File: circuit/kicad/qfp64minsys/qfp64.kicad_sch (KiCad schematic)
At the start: 0 parts

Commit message: Progress
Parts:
- added C1, C2, C4: 100nF, Capacitor_SMD:C_0805_2012Metric_Pad1.18x1.45mm_HandSolder, symbol Device:C
- added C3: 100uF, Capacitor_THT:CP_Radial_D4.0mm_P1.50mm, symbol Device:C_Polarized
- added C5, C6, C7, C8: 10nF, Capacitor_SMD:C_0805_2012Metric_Pad1.18x1.45mm_HandSolder, symbol Device:C
- added C9: 4u7F, Capacitor_Tantalum_SMD:CP_EIA-3216-18_Kemet-A, symbol Device:C
- added D1: RED, LED_SMD:LED_0805_2012Metric_Pad1.15x1.40mm_HandSolder, symbol Device:LED
- added D2: YELLOW, LED_SMD:LED_0805_2012Metric_Pad1.15x1.40mm_HandSolder, symbol Device:LED
- added J1, J6: Conn_01x05_Pin, Connector_PinSocket_2.54mm:PinSocket_1x05_P2.54mm_Vertical, symbol Connector:Conn_01x05_Pin
- added J10, J7, J9: Conn_01x09_Pin, Connector_PinSocket_2.54mm:PinSocket_1x09_P2.54mm_Vertical, symbol Connector:Conn_01x09_Pin
- added J2, J3: USB_B_Mini, Connector_USB:USB_Mini-B_Wuerth_65100516121_Horizontal, symbol Connector:USB_B_Mini
- added J4, J5: Conn_01x03_Pin, Connector_PinSocket_2.54mm:PinSocket_1x03_P2.54mm_Vertical, symbol Connector:Conn_01x03_Pin
- added J8: Conn_01x12_Pin, Connector_PinSocket_2.54mm:PinSocket_1x12_P2.54mm_Vertical, symbol Connector:Conn_01x12_Pin
- added JP1, JP2, JP3, JP4, JP5: SolderJumper_2_Open, Jumper:SolderJumper-2_P1.3mm_Open_TrianglePad1.0x1.5mm, symbol Jumper:SolderJumper_2_Open
- added R1, R2, R3, R6: 10K, Resistor_SMD:R_0805_2012Metric_Pad1.20x1.40mm_HandSolder, symbol Device:R
- added R4, R5: 330, Resistor_SMD:R_0805_2012Metric_Pad1.20x1.40mm_HandSolder, symbol Device:R
- added SW1, SW2, SW3: SW_Push, Button_Switch_THT:SW_PUSH_6mm, symbol Switch:SW_Push
- added U1: STM32F401RETx, Package_QFP:LQFP-64_10x10mm_P0.5mm, symbol MCU_ST_STM32F4:STM32F401RETx
- added U2: CH340C, Package_SO:SOIC-16_3.9x9.9mm_P1.27mm, symbol Interface_USB:CH340C
- added U3: AMS1117-3.3, Package_TO_SOT_SMD:SOT-223-3_TabPin2, symbol Regulator_Linear:AMS1117-3.3
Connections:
- new net: D2.2 (A), R5.2
- new net: JP1.1 (A), U1.19 (VDD)
- new net: C1.1, U2.4 (V3)
- new net: J3.3 (D+), U2.5 (UD+)
- new net: J3.2 (D-), U2.6 (UD-)
- new net: JP2.1 (A), U1.48 (VDD)
- new net: J6.1 (Pin_1), JP3.1 (A)
- new net: J6.2 (Pin_2), JP4.1 (A)
- new net: D1.2 (A), R4.2
- new net +5V: C3.1, J2.1 (VBUS), J3.1 (VBUS), J4.1 (Pin_1), J4.2 (Pin_2), J4.3 (Pin_3), JP3.2 (B), U2.16 (VCC), U3.3 (VI)
- new net BOOT0: R2.2, SW2.2, U1.60 (BOOT0)
- new net BOOT1: JP5.1 (A), U1.28 (PB2)
- new net BTN: R3.2, SW3.2, U1.2 (PC13)
- new net GND: C1.2, C2.2, C3.2, C4.2, C5.2, C6.2, C7.2, C8.2, C9.2, D1.1 (K), J1.3 (Pin_3), J2.5 (GND), J2.6 (Shield), J3.5 (GND), J3.6 (Shield), J5.1 (Pin_1), J5.2 (Pin_2), J5.3 (Pin_3), J6.5 (Pin_5), JP5.2 (B), SW1.1, SW2.1, SW3.1, U1.12 (VSSA), U1.18 (VSS), U1.31 (VSS), U1.47 (VSS), U1.63 (VSS), U2.1 (GND), U3.1 (GND)
- new net LED: D2.1 (K), U1.21 (PA5)
- new net NRST: J1.5 (Pin_5), R1.2, SW1.2, U1.7 (NRST)
- new net PA0: J9.7 (Pin_7), U1.14 (PA0)
- new net PA1: J9.8 (Pin_8), U1.15 (PA1)
- new net PA15: J8.1 (Pin_1), U1.50 (PA15)
- new net PA2: J9.9 (Pin_9), U1.16 (PA2)
- new net PA3: J10.1 (Pin_1), U1.17 (PA3)
- new net PA4: J10.2 (Pin_2), U1.20 (PA4)
- new net PA6: J10.3 (Pin_3), U1.22 (PA6)
- new net PA7: J10.4 (Pin_4), U1.23 (PA7)
- new net PA8: J7.1 (Pin_1), U1.41 (PA8)
- new net PB0: J10.7 (Pin_7), U1.26 (PB0)
- new net PB1: J10.8 (Pin_8), U1.27 (PB1)
- new net PB10: J10.9 (Pin_9), U1.29 (PB10)
- new net PB12: J7.9 (Pin_9), U1.33 (PB12)
- new net PB13: J7.8 (Pin_8), U1.34 (PB13)
- new net PB14: J7.7 (Pin_7), U1.35 (PB14)
- new net PB15: J7.6 (Pin_6), U1.36 (PB15)
- new net PB3: J8.6 (Pin_6), U1.55 (PB3)
- new net PB4: J8.7 (Pin_7), U1.56 (PB4)
- new net PB5: J8.8 (Pin_8), U1.57 (PB5)
- new net PB6: J8.9 (Pin_9), U1.58 (PB6)
- new net PB7: J8.10 (Pin_10), U1.59 (PB7)
- new net PB8: J8.11 (Pin_11), U1.61 (PB8)
- new net PB9: J8.12 (Pin_12), U1.62 (PB9)
- new net PC0: J9.3 (Pin_3), U1.8 (PC0)
- new net PC1: J9.4 (Pin_4), U1.9 (PC1)
- new net PC10: J8.2 (Pin_2), U1.51 (PC10)
- new net PC11: J8.3 (Pin_3), U1.52 (PC11)
- new net PC12: J8.4 (Pin_4), U1.53 (PC12)
- new net PC14: J9.1 (Pin_1), U1.3 (PC14)
- new net PC15: J9.2 (Pin_2), U1.4 (PC15)
- new net PC2: J9.5 (Pin_5), U1.10 (PC2)
- new net PC3: J9.6 (Pin_6), U1.11 (PC3)
- new net PC4: J10.5 (Pin_5), U1.24 (PC4)
- new net PC5: J10.6 (Pin_6), U1.25 (PC5)
- new net PC6: J7.5 (Pin_5), U1.37 (PC6)
- new net PC7: J7.4 (Pin_4), U1.38 (PC7)
- new net PC8: J7.3 (Pin_3), U1.39 (PC8)
- new net PC9: J7.2 (Pin_2), U1.40 (PC9)
- new net PD2: J8.5 (Pin_5), U1.54 (PD2)
- new net RXD: J6.4 (Pin_4), U1.43 (PA10), U2.2 (TXD)
- new net SWCLK: J1.2 (Pin_2), U1.49 (PA14)
- new net SWDIO: J1.4 (Pin_4), U1.46 (PA13)
- new net TXD: J6.3 (Pin_3), U1.42 (PA9), U2.3 (RXD)
- new net USBDM: J2.2 (D-), U1.44 (PA11)
- new net USBDP: J2.3 (D+), R6.2, U1.45 (PA12)
- new net VCAP: C9.1, U1.30 (VCAP1)
- new net VDD: C2.1, C4.1, C5.1, C6.1, C7.1, C8.1, J1.1 (Pin_1), JP1.2 (B), JP2.2 (B), JP4.2 (B), R1.1, R2.1, R3.1, R4.1, R5.1, R6.1, U1.1 (VBAT), U1.13 (VREF+), U1.32 (VDD), U1.64 (VDD), U3.2 (VO)
- no-connect marks 0 -> 11

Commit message: Coba Pesan
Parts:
- removed C3: 100uF, Capacitor_THT:CP_Radial_D4.0mm_P1.50mm, symbol Device:C_Polarized
- removed C7, C8: 10nF, Capacitor_SMD:C_0805_2012Metric_Pad1.18x1.45mm_HandSolder, symbol Device:C
- removed J6: Conn_01x05_Pin, Connector_PinSocket_2.54mm:PinSocket_1x05_P2.54mm_Vertical, symbol Connector:Conn_01x05_Pin
- removed JP3, JP4: SolderJumper_2_Open, Jumper:SolderJumper-2_P1.3mm_Open_TrianglePad1.0x1.5mm, symbol Jumper:SolderJumper_2_Open
- removed R2: 10K, Resistor_SMD:R_0805_2012Metric_Pad1.20x1.40mm_HandSolder, symbol Device:R
- removed SW1, SW2: SW_Push, Button_Switch_THT:SW_PUSH_6mm, symbol Switch:SW_Push
- added H1, H2, H3, H4: MountingHole, MountingHole:MountingHole_2.2mm_M2, symbol Mechanical:MountingHole
- added J1, J6, J7: Conn_01x03_Pin, Connector_PinHeader_2.54mm:PinHeader_1x03_P2.54mm_Vertical, symbol Connector:Conn_01x03_Pin
- J10: renamed from J8; footprint Connector_PinSocket_2.54mm:PinSocket_1x12_P2.54mm_Vertical -> Connector_PinHeader_2.54mm:PinHeader_1x12_P2.54mm_Vertical
- J11: renamed from J9; footprint Connector_PinSocket_2.54mm:PinSocket_1x09_P2.54mm_Vertical -> Connector_PinHeader_2.54mm:PinHeader_1x09_P2.54mm_Vertical
- J12: renamed from J10; footprint Connector_PinSocket_2.54mm:PinSocket_1x09_P2.54mm_Vertical -> Connector_PinHeader_2.54mm:PinHeader_1x09_P2.54mm_Vertical
- J3: renamed from J1; footprint Connector_PinSocket_2.54mm:PinSocket_1x05_P2.54mm_Vertical -> Connector_PinHeader_2.54mm:PinHeader_1x05_P2.54mm_Vertical
- J4: footprint Connector_PinSocket_2.54mm:PinSocket_1x03_P2.54mm_Vertical -> Connector_PinHeader_2.54mm:PinHeader_1x03_P2.54mm_Vertical
- J8: renamed from J5; footprint Connector_PinSocket_2.54mm:PinSocket_1x03_P2.54mm_Vertical -> Connector_PinHeader_2.54mm:PinHeader_1x03_P2.54mm_Vertical
- J9: renamed from J7; footprint Connector_PinSocket_2.54mm:PinSocket_1x09_P2.54mm_Vertical -> Connector_PinHeader_2.54mm:PinHeader_1x09_P2.54mm_Vertical
- JP1, JP2: footprint Jumper:SolderJumper-2_P1.3mm_Open_TrianglePad1.0x1.5mm -> Jumper:SolderJumper-2_P1.3mm_Open_RoundedPad1.0x1.5mm
- JP3: renamed from JP5; footprint Jumper:SolderJumper-2_P1.3mm_Open_TrianglePad1.0x1.5mm -> Jumper:SolderJumper-2_P1.3mm_Open_RoundedPad1.0x1.5mm
- renumbered C9 to C1, C1 to C2, C4 to C3, C5 to C4, C6 to C5, C2 to C6, J3 to J2, J2 to J5, R4 to R2, R5 to R3, R3 to R4, R6 to R5, SW3 to SW1
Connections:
- net BOOT0: now also J1.2 (Pin_2)
- net GND: now also J1.3 (Pin_3), J7.3 (Pin_3)
- net RXD: now also J7.2 (Pin_2)
- net TXD: now also J7.1 (Pin_1)
- net VDD: now also J1.1 (Pin_1), J6.1 (Pin_1), J6.2 (Pin_2), J6.3 (Pin_3)
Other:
- moved on the sheet: C1, C2, C3, C4, C5, C6, D1, D2, J10, J11, J12, J2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

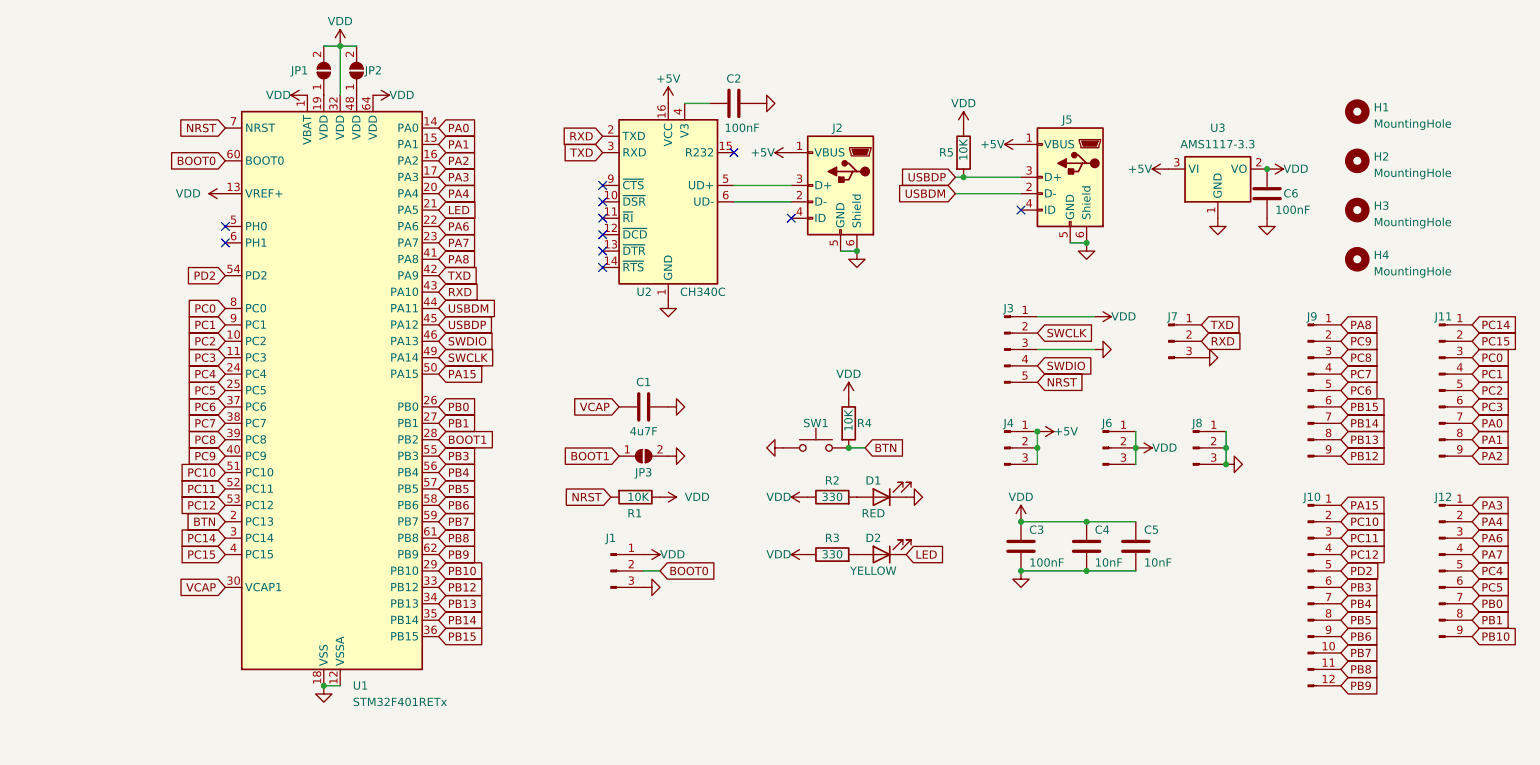
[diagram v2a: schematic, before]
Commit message: Update PCB to be Smaller
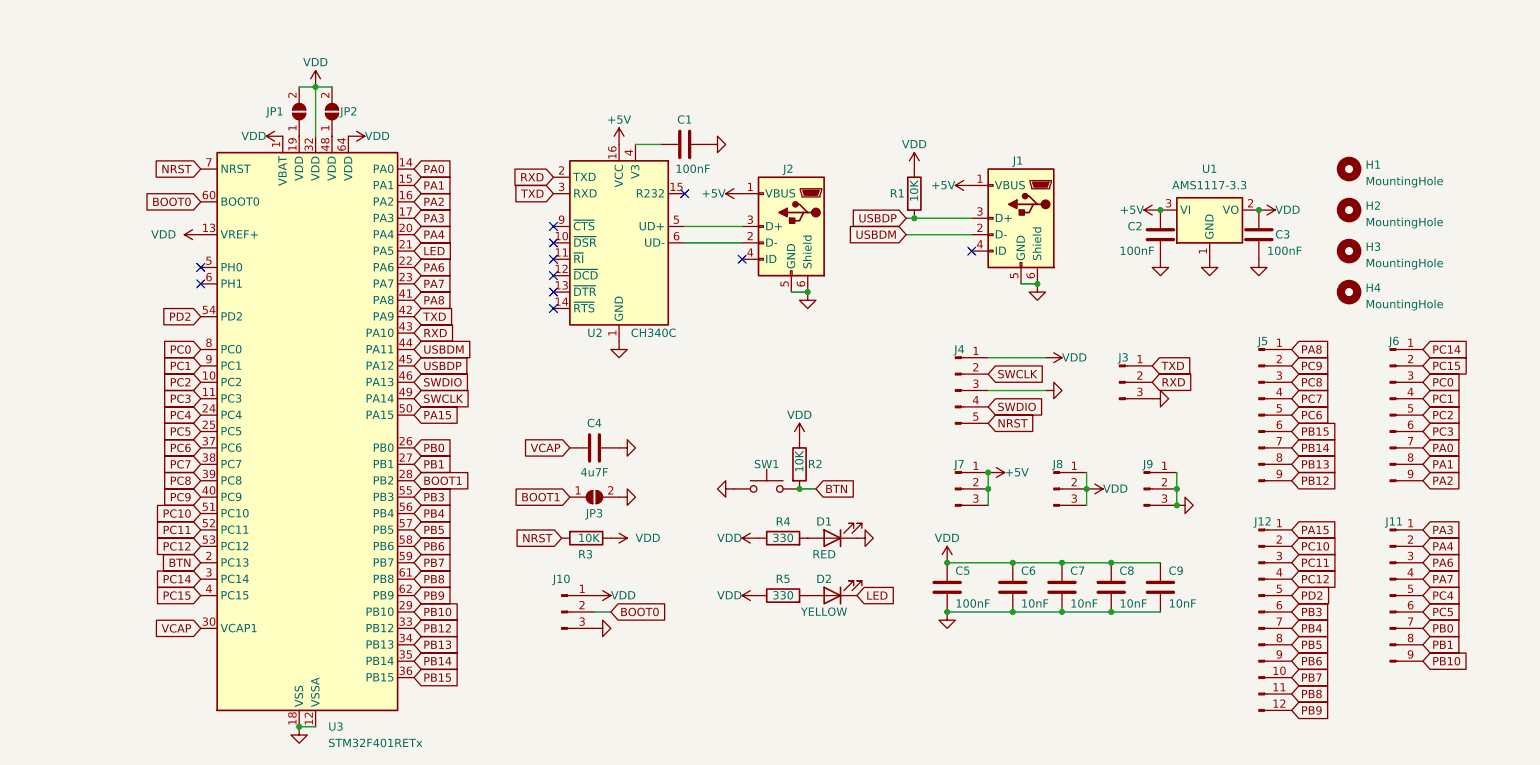
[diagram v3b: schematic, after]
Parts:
- added C2: 100nF, Capacitor_SMD:C_0805_2012Metric_Pad1.18x1.45mm_HandSolder, symbol Device:C
- added C8, C9: 10nF, Capacitor_SMD:C_0805_2012Metric_Pad1.18x1.45mm_HandSolder, symbol Device:C
- H1, H2, H3, H4: footprint MountingHole:MountingHole_2.2mm_M2 -> MountingHole:MountingHole_2.1mm
- renumbered C2 to C1, C6 to C3, C1 to C4, C3 to C5, C4 to C6, C5 to C7, J5 to J1, J1 to J10, J12 to J11, J10 to J12, J7 to J3, J3 to J4, J9 to J5, J11 to J6, J4 to J7, J6 to J8, J8 to J9, R5 to R1, R4 to R2, R1 to R3, R2 to R4, R3 to R5, U3 to U1, U1 to U3
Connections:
- net +5V: now also C2.1
- net GND: now also C2.2, C8.2, C9.2
- net VDD: now also C8.1, C9.1
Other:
- moved on the sheet: C1, C3, C4, C5, C6, C7, D1, D2, J1, J10, J11, J12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

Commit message: Update PCB LQFP64
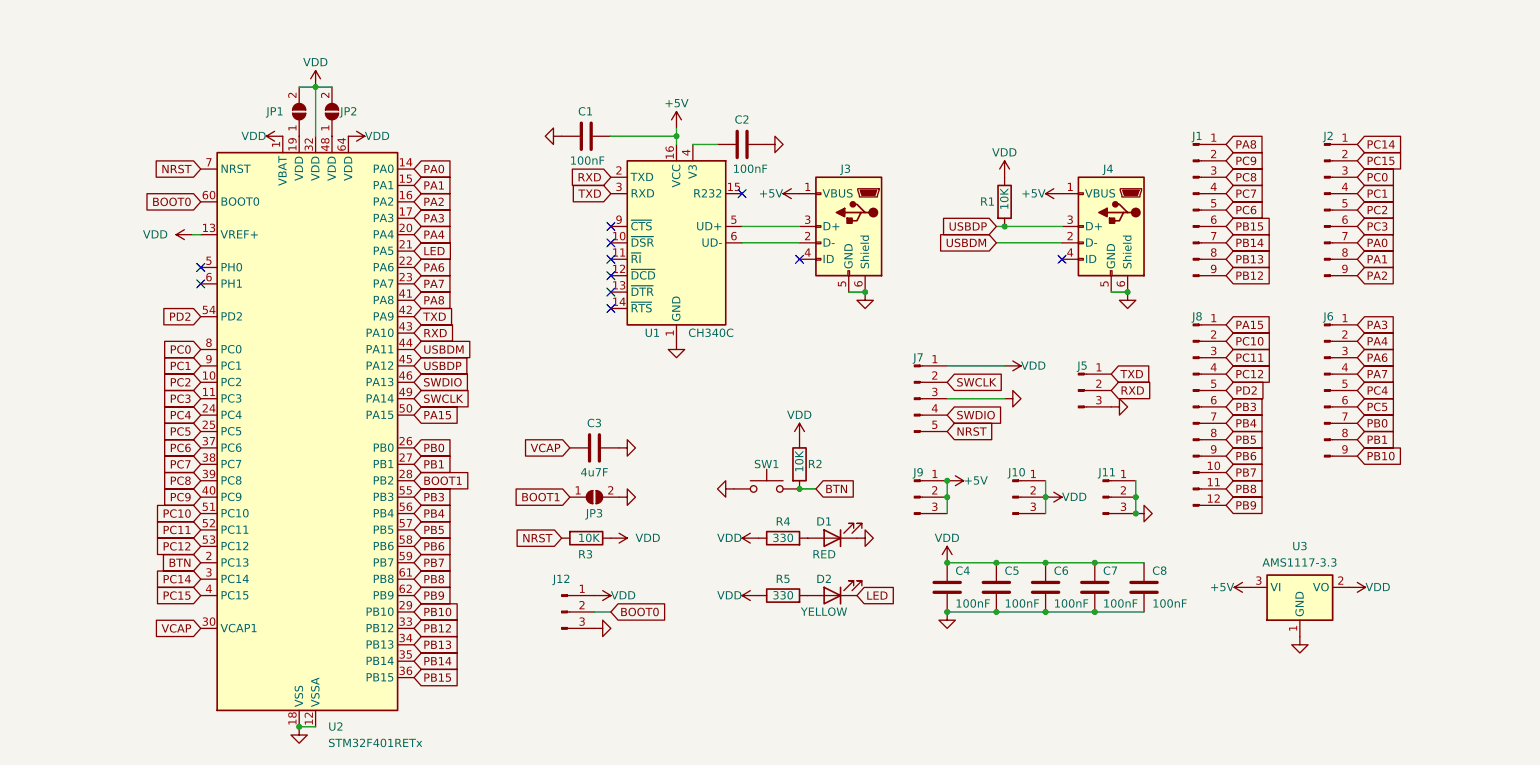
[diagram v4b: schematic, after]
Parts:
- removed C2, C3: 100nF, Capacitor_SMD:C_0805_2012Metric_Pad1.18x1.45mm_HandSolder, symbol Device:C
- removed H1, H2, H3, H4: MountingHole, MountingHole:MountingHole_2.1mm, symbol Mechanical:MountingHole
- added C8: 100nF, Capacitor_SMD:C_0805_2012Metric_Pad1.18x1.45mm_HandSolder, symbol Device:C
- C1: renamed from C9; value 10nF -> 100nF
- C5: renamed from C6; value 10nF -> 100nF
- C6: renamed from C7; value 10nF -> 100nF
- C7: renamed from C8; value 10nF -> 100nF
- renumbered C1 to C2, C4 to C3, C5 to C4, J5 to J1, J8 to J10, J9 to J11, J10 to J12, J6 to J2, J2 to J3, J1 to J4, J3 to J5, J11 to J6, J4 to J7, J12 to J8, J7 to J9, U2 to U1, U3 to U2, U1 to U3
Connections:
- net +5V: now also C1.1
- net GND: now also C8.2
- net VDD: now also C8.1; no longer C1.1
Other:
- moved on the sheet: C1, C2, C5, C6, C7, J1, J10, J11, J2, J3, J4, J5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
